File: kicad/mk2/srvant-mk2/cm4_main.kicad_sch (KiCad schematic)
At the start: 0 parts

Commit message: merge cm4 into one page, basic interconnection
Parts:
- added C19, C20: 10u 35v, Capacitor_SMD:C_0805_2012Metric, symbol Device:C
- added C21, C22, C24, C25, C26, C28, C58, C63, C64, C66, C68, C72, C73: 10u, Capacitor_SMD:C_0805_2012Metric, symbol Device:C
- added C23, C27, C29: 100n, Capacitor_SMD:C_0805_2012Metric, symbol Device:C
- added C35, C36, C37, C74, C75, C76 (x2), C77, C78, C79: 100n, Capacitor_SMD:C_0402_1005Metric, symbol Device:C
- added C62: 100u, Capacitor_Tantalum_SMD:CP_EIA-7343-31_Kemet-D, symbol Device:CP
- added C70, C71: 27p, Capacitor_SMD:C_0402_1005Metric, symbol Device:C
- added D2: LED Green, LED_SMD:LED_0603_1608Metric, symbol Device:LED
- added D3: LED Red, LED_SMD:LED_0603_1608Metric, symbol Device:LED
- added FB6: 220R, Resistor_SMD:R_0402_1005Metric, symbol Device:FerriteBead_Small
- added H1, H2, H3: MountingHole, MountingHole:MountingHole_2.5mm_Pad_TopOnly, symbol Mechanical:MountingHole
- added J2: Bus_M.2_Socket_M, footprints:1-2199230-5, symbol Connector:Bus_M.2_Socket_M
- added J3: HDMI connector, footprints:HDMI-10029449-001RLF, symbol CM4IO:HDMI_A_1.4
- added J3: Conn_02x05_Odd_Even, Connector_PinHeader_2.54mm:PinHeader_2x05_P2.54mm_Vertical, symbol Connector_Generic:Conn_02x05_Odd_Even
- added J4: ARJM11, Connector_RJ:RJ45_Wuerth_7499111446_Horizontal, symbol Connector:ARJM11
- added J4: 690-008-221-904, CM4:MOLEX_USB_67298-4090, symbol CM4IO:USB_67298-4090
- added L2: SRN6045TA-3R3Y, Inductor_SMD:L_Bourns_SRN6045TA, symbol pspice:INDUCTOR
- added Module1: ComputeModule4, CM4IO:Raspberry-Pi-4-Compute-Module, symbol CM4IO:ComputeModule4-CM4
- added R11, R12: 1K, Resistor_SMD:R_0402_1005Metric, symbol Device:R
- added R13, R14: 470R, Resistor_SMD:R_0402_1005Metric, symbol Device:R
- added R48: 15K/1%, Resistor_SMD:R_0402_1005Metric, symbol Device:R
- added R51, R52: 2.2K/1%, Resistor_SMD:R_0402_1005Metric, symbol Device:R
- added R53, R55, R56, R58: 36K/1%, Resistor_SMD:R_0402_1005Metric, symbol Device:R
- added R57: 12K/1%, Resistor_SMD:R_0402_1005Metric, symbol Device:R
- added R6: 100K 1%, Resistor_SMD:R_0402_1005Metric, symbol Device:R
- added R7: 22K 1%, Resistor_SMD:R_0402_1005Metric, symbol Device:R
- added TP4: TestPoint, TestPoint:TestPoint_Pad_1.5x1.5mm, symbol Connector:TestPoint
- added TP5, TP6, TP7, TP9: TestPoint, TestPoint:TestPoint_Pad_2.0x2.0mm, symbol Connector:TestPoint
- added U10: RT9742SNGV, Package_TO_SOT_SMD:SOT-23, symbol CM4IO:RT9742SNGV
- added U10: FSUSB42MUX, srvant:FSUSB42UMX, symbol CM4IO:FSUSB42MX
- added U11: USB2514B-I/M2, Package_DFN_QFN:QFN-36-1EP_6x6mm_P0.5mm_EP3.7x3.7mm, symbol Interface_USB:USB2514B_Bi
- added U3: TLV62585DRLR, TLV62585DRLR:DRL0006A, symbol TLV62585DRLR:TLV62585DRLR
- added U7: 74LVC1G07SE-7, Package_TO_SOT_SMD:SOT-353_SC-70-5, symbol CM4IO:74LVC1G07_copy
- added U8: AP22653W6, Package_TO_SOT_SMD:SOT-23-6, symbol CM4IO:AP2553W6
- added U8, U9: TPD4EUSB30, Package_SON:USON-10_2.5x1.0mm_P0.5mm, symbol CM4IO:TPD4EUSB30
- added Y2: 24MHz, srvant:LFXTAL-25MHz, symbol Device:Crystal_GND24
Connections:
- new net: R48.1, U8.5 (ILIM)
- new net: D3.1 (K), R12.1, TP9.1
- new net: J4.14 (LED1-), R14.1
- new net: J4.12 (LED2-), R13.1
- new net: C35.1, C76.1, J4.5 (CT), J4.6 (CT)
- new net: FB6.1, J4.SH
- new net: R55.1, U11.22 (SDA/SMBDATA/NON_REM1)
- new net: R51.2, R52.1, U10.2 (SEL)
- new net: L2.1, U3.2 (SW)
- new net: R12.2, U7.4
- new net: R57.2, U11.35 (RBIAS)
- new net: Module1.21 (PI_nLED_Activity), R11.2
- new net: D2.1 (K), R11.1
- new net: R56.1, U11.28 (SUSP_IND/LOCAL_PWR/NON_REM0)
- new net: R53.1, U11.24 (SCL/SMBCLK/CFG_SEL0)
- new net: R58.1, U11.25 (HS_IND/CFG_SEL1)
- new net +1.8v: Module1.88 (+1.8v_(Output)), Module1.90 (+1.8v_(Output))
- new net +3.3v: C72.1, C73.1, C74.1, C75.1, C76.1, C77.1, C78.1, C79.1, D2.2 (A), D3.2 (A), J4.11 (LED2+), J4.13 (LED1+), Module1.78 (GPIO_VREF(1.8v/3.3v_Input)), Module1.84 (+3.3v_(Output)), Module1.86 (+3.3v_(Output)), U10.1 (VCC), U11.10 (VDDA33), U11.15 (VDD33), U11.23 (VDD33), U11.27 (VBUS_DET), U11.29 (VDDA33), U11.36 (VDDA33), U11.5 (VDDA33), U7.5 (VCC)
- new net +3V3 PCIe: C21.1, C22.1, C23.1, C24.1, C25.1, C26.1, C27.1, C28.1, C29.1, J2.12 (3.3V), J2.14 (3.3V), J2.16 (3.3V), J2.18 (3.3V), J2.2 (3.3V), J2.4 (3.3V), J2.70 (3.3V), J2.72 (3.3V), J2.74 (3.3V), L2.2, R6.1, TP4.1
- new net +5v: C19.1, C20.1, C36.1, C58.1, Module1.77 (+5v_(Input)), Module1.79 (+5v_(Input)), Module1.81 (+5v_(Input)), Module1.83 (+5v_(Input)), Module1.85 (+5v_(Input)), Module1.87 (+5v_(Input)), U10.1 (IN), U3.3 (VIN), U3.4 (EN), U8.1 (IN)
- new net 3V3P_FB: R6.2, R7.1, TP5.1, U3.5 (FB)
- new net BT_nDis: Module1.91 (BT_nDisable)
- new net CAM0_C_N: Module1.140 (CAM0_C_N)
- new net CAM0_C_P: Module1.142 (CAM0_C_P)
- new net CAM0_D0_N: Module1.128 (CAM0_D0_N)
- new net CAM0_D0_P: Module1.130 (CAM0_D0_P)
- new net CAM0_D1_N: Module1.134 (CAM0_D1_N)
- new net CAM0_D1_P: Module1.136 (CAM0_D1_P)
- new net CAM1_C_N: Module1.127 (CAM1_C_N)
- new net CAM1_C_P: Module1.129 (CAM1_C_P)
- new net CAM1_D0_N: Module1.115 (CAM1_D0_N)
- new net CAM1_D0_P: Module1.117 (CAM1_D0_P)
- new net CAM1_D1_N: Module1.121 (CAM1_D1_N)
- new net CAM1_D1_P: Module1.123 (CAM1_D1_P)
- new net CAM1_D2_N: Module1.133 (CAM1_D2_N)
- new net CAM1_D2_P: Module1.135 (CAM1_D2_P)
- new net CAM1_D3_N: Module1.139 (CAM1_D3_N)
- new net CAM1_D3_P: Module1.141 (CAM1_D3_P)
- new net DSI0_C_N: Module1.169 (DSI0_C_N)
- new net DSI0_C_P: Module1.171 (DSI0_C_P)
- new net DSI0_D0_N: Module1.157 (DSI0_D0_N)
- new net DSI0_D0_P: Module1.159 (DSI0_D0_P)
- new net DSI0_D1_N: Module1.163 (DSI0_D1_N)
- new net DSI0_D1_P: Module1.165 (DSI0_D1_P)
- new net DSI1_C_N: Module1.187 (DSI1_C_N)
- new net DSI1_C_P: Module1.189 (DSI1_C_P)
- new net DSI1_D0_N: Module1.175 (DSI1_D0_N)
- new net DSI1_D0_P: Module1.177 (DSI1_D0_P)
- new net DSI1_D1_N: Module1.181 (DSI1_D1_N)
- new net DSI1_D1_P: Module1.183 (DSI1_D1_P)
- new net DSI1_D2_N: Module1.193 (DSI1_D2_N)
- new net DSI1_D2_P: Module1.195 (DSI1_D2_P)
- new net DSI1_D3_N: Module1.194 (DSI1_D3_N)
- new net DSI1_D3_P: Module1.196 (DSI1_D3_P)
- new net EEPROM_nWP: Module1.20 (EEPROM_nWP)
- new net ETH_LEDG: Module1.17 (Ethernet_nLED2(3.3v)), R13.2
- new net ETH_LEDY: Module1.15 (Ethernet_nLED3(3.3v)), R14.2
- new net GLOBAL_EN: Module1.99 (Global_EN)
- new net GND: C19.2, C20.2, C21.2, C22.2, C23.2, C24.2, C25.2, C26.2, C27.2, C28.2, C29.2, C35.2, C36.2, C37.2, C58.2, C62.2, C63.2, C64.2, C66.2, C68.2, C70.2, C71.2, C72.2, C73.2, C74.2, C75.2, C76.2, C76.2, C77.2, C78.2, C79.2, FB6.2, J2.1 (GND), J2.15 (GND), J2.21 (GND), J2.27 (GND), J2.3 (GND), J2.33 (GND), J2.39 (GND), J2.45 (GND), J2.51 (GND), J2.57 (GND), J2.71 (GND), J2.73 (GND), J2.75 (GND), J2.9 (GND), J3.11 (CKS), J3.17 (GND), J3.2 (D2S), J3.5 (D1S), J3.7 (Pin_7), J3.8 (D0S), J3.8 (Pin_8), J3.SH1 (SH), J3.SH2 (SH), J3.SH3 (SH), J3.SH4 (SH), J4.4 (GND`), J4.8 (GND), J4.MT1, J4.MT2, J4.MT3, J4.MT4, Module1.1 (GND), Module1.107 (GND), Module1.108 (GND), Module1.113 (GND), Module1.114 (GND), Module1.119 (GND), Module1.120 (GND), Module1.125 (GND), Module1.126 (GND), Module1.13 (GND), Module1.131 (GND), Module1.132 (GND), Module1.137 (GND), Module1.138 (GND), Module1.14 (GND), Module1.144 (GND), Module1.150 (GND), Module1.155 (GND), Module1.156 (GND), Module1.161 (GND), Module1.162 (GND), Module1.167 (GND), Module1.168 (GND), Module1.173 (GND), Module1.174 (GND), Module1.179 (GND), Module1.180 (GND), Module1.185 (GND), Module1.186 (GND), Module1.191 (GND), Module1.192 (GND), Module1.197 (GND), Module1.198 (GND), Module1.2 (GND), Module1.22 (GND), Module1.23 (GND), Module1.32 (GND), Module1.33 (GND), Module1.42 (GND), Module1.43 (GND), Module1.52 (GND), Module1.53 (GND), Module1.59 (GND), Module1.60 (GND), Module1.65 (GND), Module1.66 (GND), Module1.7 (GND), Module1.71 (GND), Module1.74 (GND), Module1.8 (GND), Module1.98 (GND), R48.2, R52.2, R53.2, R55.2, R56.2, R57.1, R58.2, R7.2, U10.10 (nOE), U10.3 (GND), U10.5 (GND), U11.37 (VSS), U3.1 (GND), U7.3 (GND), U8.2 (GND), U8.3 (GND), U8.8 (GND), U9.3 (GND), U9.8 (GND), Y2.2, Y2.4
- new net GPIO12: Module1.31 (GPIO12)
- new net GPIO13: Module1.28 (GPIO13)
- new net GPIO16: Module1.29 (GPIO16)
- new net GPIO17: Module1.50 (GPIO17)
- new net GPIO18: Module1.49 (GPIO18)
- new net GPIO19: Module1.26 (GPIO19)
- new net GPIO2: Module1.58 (GPIO2)
- new net GPIO20: Module1.27 (GPIO20)
- new net GPIO21: Module1.25 (GPIO21)
- new net GPIO22: Module1.46 (GPIO22)
- new net GPIO23: Module1.47 (GPIO23)
- new net GPIO24: Module1.45 (GPIO24)
- new net GPIO25: Module1.41 (GPIO25)
- new net GPIO26: Module1.24 (GPIO26)
- new net GPIO27: Module1.48 (GPIO27)
- new net GPIO3: Module1.56 (GPIO3)
- new net GPIO4: Module1.54 (GPIO4)
- new net GPIO5: Module1.34 (GPIO5)
- new net GPIO6: Module1.30 (GPIO6)
- new net GPIO7: Module1.37 (GPIO7)
- new net GPIO8: Module1.39 (GPIO8)
- new net GPIO9: Module1.40 (GPIO9)
- new net HD1_N: J4.2 (D-`), U11.1 (USBDM_DN1/PRT_DIS_M1)
- new net HD1_P: J4.3 (D+`), U11.2 (USBDP_DN1/PRT_DIS_P1)
- new net HD2_N: J4.6 (D-), U11.3 (USBDM_DN2/PRT_DIS_M2)
- new net HD2_P: J4.7 (D+), U11.4 (USBDP_DN2/PRT_DIS_P2)
- new net HD3_N: J3.3 (Pin_3), U11.6 (USBDM_DN3/PRT_DIS_M3)
- new net HD3_P: J3.5 (Pin_5), U11.7 (USBDP_DN3/PRT_DIS_P3)
- new net HD4_N: J3.4 (Pin_4), U11.8 (USBDM_DN4/PRT_DIS_M4)
- new net HD4_P: J3.6 (Pin_6), U11.9 (USBDP_DN4/PRT_DIS_P4)
- new net HDMI0_CEC: J3.13 (CEC), Module1.151 (HDMI0_CEC)
- new net HDMI0_CK_N: J3.12 (CK-), Module1.190 (HDMI0_CLK_N)
- new net HDMI0_CK_P: J3.10 (CK+), Module1.188 (HDMI0_CLK_P)
- new net HDMI0_D0_N: J3.9 (D0-), Module1.184 (HDMI0_TX0_N)
- new net HDMI0_D0_P: J3.7 (D0+), Module1.182 (HDMI0_TX0_P)
- new net HDMI0_D1_N: J3.6 (D1-), Module1.178 (HDMI0_TX1_N)
- new net HDMI0_D1_P: J3.4 (D1+), Module1.176 (HDMI0_TX1_P)
- new net HDMI0_D2_N: J3.3 (D2-), Module1.172 (HDMI0_TX2_N)
- new net HDMI0_D2_P: J3.1 (D2+), Module1.170 (HDMI0_TX2_P)
- new net HDMI0_HOTPLUG: J3.19 (HPD/HEAC-), Module1.153 (HDMI0_HOTPLUG)
- new net HDMI0_SCL: J3.15 (SCL), Module1.200 (HDMI0_SCL)
- new net HDMI0_SDA: J3.16 (SDA), Module1.199 (HDMI0_SDA)
- new net HDMI1_CEC: Module1.149 (HDMI1_CEC)
- new net HDMI1_CK_N: Module1.166 (HDMI1_CLK_N)
- new net HDMI1_CK_P: Module1.164 (HDMI1_CLK_P)
- new net HDMI1_D0_N: Module1.160 (HDMI1_TX0_N)
- new net HDMI1_D0_P: Module1.158 (HDMI1_TX0_P)
- new net HDMI1_D1_N: Module1.154 (HDMI1_TX1_N)
- new net HDMI1_D1_P: Module1.152 (HDMI1_TX1_P)
- new net HDMI1_D2_N: Module1.148 (HDMI1_TX2_N)
- new net HDMI1_D2_P: Module1.146 (HDMI1_TX2_P)
- new net HDMI1_HOTPLUG: Module1.143 (HDMI1_HOTPLUG)
- new net HDMI1_SCL: Module1.147 (HDMI1_SCL)
- new net HDMI1_SDA: Module1.145 (HDMI1_SDA)
- new net HDMI_5v: C37.1, J3.18 (+5V), U10.2 (OUT)
- new net HOST_RUN_PG: Module1.92 (RUN_PG)
- new net HOST_SCL_2: Module1.38 (GPIO11)
- new net HOST_SDA_2: Module1.44 (GPIO10)
- new net HOST_UART_RX: Module1.55 (GPIO14)
- new net HOST_UART_TX: Module1.51 (GPIO15)
- new net HOST_USB_N: U10.8 (HSD1_M)
- new net HOST_USB_P: U10.9 (HSD1_P)
- new net HOST_USB_SELECT: R51.1
- new net HOST_nRPIBOOT: Module1.93 (nRPIBOOT)
- new net ID_SC: Module1.35 (ID_SC)
- new net ID_SD: Module1.36 (ID_SD)
- new net PCIE_CLK_N: J2.53 (REFCLKn), Module1.112 (PCIe_CLK_N)
- new net PCIE_CLK_P: J2.55 (REFCLKp), Module1.110 (PCIe_CLK_P)
- new net PCIE_CLK_nREQ: J2.52 (~CLKREQ), Module1.102 (PCIe_CLK_nREQ)
- new net PCIE_RX_N: J2.41 (PERn0/SATA-B+), Module1.118 (PCIe_RX_N)
- new net PCIE_RX_P: J2.43 (PERp0/SATA-B-), Module1.116 (PCIe_RX_P)
- new net PCIE_TX_N: J2.47 (PETn0/SATA-A-), Module1.124 (PCIe_TX_N)
- new net PCIE_TX_P: J2.49 (PETp0/SATA-A+), Module1.122 (PCIe_TX_P)
- new net PCIE_nRST: J2.50 (~PERST), Module1.109 (PCIe_nRST)
- new net PCIe_nCLKREQ: TP6.1
- new net PCIe_nRST: TP7.1
- new net PWR1: U11.12 (PRTPWR1/BC_EN1), U8.3 (EN)
- new net SCL0: Module1.80 (SCL0)
- new net SDA0: Module1.82 (SDA0)
- new net SD_CLK: Module1.57 (SD_CLK)
- new net SD_DAT0: Module1.63 (SD_DAT0)
- new net SD_DAT1: Module1.67 (SD_DAT1)
- new net SD_DAT2: Module1.69 (SD_DAT2)
- new net SD_DAT3: Module1.61 (SD_DAT3)
- new net SD_PWR_ON: Module1.75 (SD_PWR_ON)
- new net SYNC_IN: Module1.16 (Ethernet_SYNC_IN(1.8v))
- new net SYNC_OUT: Module1.18 (Ethernet_SYNC_OUT(1.8v))
- new net TRD0_N: J4.2 (TD1-), Module1.10 (Ethernet_Pair0_N), U9.4 (D2+), U9.7
- new net TRD0_P: J4.1 (TD1+), Module1.12 (Ethernet_Pair0_P), U9.5 (D2-), U9.6
- new net TRD1_N: J4.4 (TD2-), Module1.6 (Ethernet_Pair1_N), U9.2 (D1-), U9.9
- new net TRD1_P: J4.3 (TD2+), Module1.4 (Ethernet_Pair1_P), U9.1 (D1+), U9.10
- new net TRD2_N: J4.8 (TD3-), Module1.9 (Ethernet_Pair2_N), U8.4 (D2+), U8.7
- new net TRD2_P: J4.7 (TD3+), Module1.11 (Ethernet_Pair2_P), U8.5 (D2-), U8.6
- new net TRD3_N: J4.10 (TD4-), Module1.5 (Ethernet_Pair3_N), U8.2 (D1-), U8.9
- new net TRD3_P: J4.9 (TD4+), Module1.3 (Ethernet_Pair3_P), U8.1 (D1+), U8.10
- new net TV_OUT: Module1.111 (VDAC_COMP)
- new net USB2_N: Module1.103 (USB2_N), U10.4 (D_N)
- new net USB2_P: Module1.105 (USB2_P), U10.3 (D_P)
- new net USBH_N: U10.6 (HSD0_M), U11.30 (USBDM_UP)
- new net USBH_P: U10.7 (HSD0_P), U11.31 (USBDP_UP)
- new net USBOTG_ID: Module1.101 (USB_OTG_ID)
- new net VBUS: C62.1, C63.1, C64.1, C66.1, C68.1, J3.1 (Pin_1), J3.2 (Pin_2), J4.1 (VBUS`), J4.5 (VBUS), U8.6 (OUT)
- new net WL_nDis: Module1.89 (WL_nDisable)
- new net XTALIN: C70.1, U11.33 (XTALIN/CLKIN), Y2.1
- new net XTALOUT: C71.1, U11.32 (XTALOUT), Y2.3
- new net nEXTRST: Module1.100 (nEXTRST), U11.26 (RESET_N)
- new net nOCS1: U11.13 (OCS_N1), U11.17 (OCS_N2), U11.19 (OCS_N3), U11.21 (OCS_N4), U8.4 (nFault)
- new net nPWR_LED: Module1.95 (nPI_LED_PWR), U7.2
- no-connect marks 0 -> 35
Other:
- removed sheet CM4_GPIO
- removed sheet cm4-high-speed
- note added: "3.3v @ 3A PSU For PCIE"
- note added: "Activity LED"
- note added: "Current Limit switch"
- note added: "Ethernet"
- note added: "Ethernet POE Protection"
- note added: "Expansion USB connector"
- note added: "HDMI power"
- note added: "M.2 Socket 3 (M-Key) PCIe x1"
- note added: "MOUNT HOLES"
- note added: "PCIe power"
- note added: "PWR LED"
- note added: "Stacked USB connectors"
- note added: "TESTPOINTS"
- note added: "TODO: EEPROM_nWP: use OR gate with the DIP switch and BMC pin BMC_HOST_USB_SELECT: use OR gate with the DIP switch and BMC pin"
- note added: "USB 2.0 Hub"
- note added: "USB power"

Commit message: more progress
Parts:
- removed R51: 2.2K/1%, Resistor_SMD:R_0402_1005Metric, symbol Device:R
- J7: renamed from J4; value 690-008-221-904 -> USB[690-008-221-904]; footprint CM4:MOLEX_USB_67298-4090 -> footprints:MOLEX_USB_67298-4090; Field4 Farnell -> (none); Field5 2751688 -> (none); Field6 690-008-221-904 -> (none); Field7 EDAC -> (none); Field8 UCON00727 -> (none); farnell# (none) -> 2751688
- U16: renamed from U10; footprint srvant:FSUSB42UMX -> footprints:FSUSB42UMX
- Y3: renamed from Y2; footprint srvant:LFXTAL-25MHz -> footprints:LFXTAL-25MHz
- renumbered C21 to C100, C27 to C101, C29 to C102, C23 to C103, C76 to C104, C35 to C105, C19 to C75, C58 to C76, C20 to C77, C36 to C78, C37 to C79, C62 to C80, C63 to C81, C64 to C82, C22 to C83, C66 to C84, C24 to C85, C68 to C86, C26 to C87, C70 to C88, C71 to C89, C72 to C90, C73 to C91, C74 to C92, C75 to C93, C76 to C94, C77 to C95, C78 to C96, C79 to C97, C25 to C98, C28 to C99, D2 to D7, D3 to D8, J3 to J10, J3 to J6, J2 to J8, J4 to J9, L2 to L3, R48 to R54, R6 to R55, R7 to R56, R52 to R58, R53 to R59, R11 to R60, R55 to R61, R56 to R62, R57 to R63, R58 to R64, R12 to R65, R13 to R66, R14 to R67, TP9 to TP11, TP4 to TP12, TP5 to TP13, TP6 to TP14, TP7 to TP15, U10 to U13, U8 to U14, U3 to U15, U11 to U17, U7 to U18, U8 to U19, U9 to U20
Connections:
- net USBOTG_ID is gone; now on net USB_DEMUX_SELECT: Module1.101 (USB_OTG_ID)
- net USB_DEMUX_SELECT: now reaches R58.1, U16.2 (SEL)
- net +3.3v renamed +3.3v_HOST
- net +5v renamed +5v_HOST
- net BT_nDis renamed HOST_BT_nDis
- net CAM0_C_N: no longer names the net of Module1.140 (CAM0_C_N)
- net CAM0_C_P: no longer names the net of Module1.142 (CAM0_C_P)
- net CAM0_D0_N: no longer names the net of Module1.128 (CAM0_D0_N)
- net CAM0_D0_P: no longer names the net of Module1.130 (CAM0_D0_P)
- net CAM0_D1_N: no longer names the net of Module1.134 (CAM0_D1_N)
- net CAM0_D1_P: no longer names the net of Module1.136 (CAM0_D1_P)
- net CAM1_C_N: no longer names the net of Module1.127 (CAM1_C_N)
- net CAM1_C_P: no longer names the net of Module1.129 (CAM1_C_P)
- net CAM1_D0_N: no longer names the net of Module1.115 (CAM1_D0_N)
- net CAM1_D0_P: no longer names the net of Module1.117 (CAM1_D0_P)
- net CAM1_D1_N: no longer names the net of Module1.121 (CAM1_D1_N)
- net CAM1_D1_P: no longer names the net of Module1.123 (CAM1_D1_P)
- net CAM1_D2_N: no longer names the net of Module1.133 (CAM1_D2_N)
- net CAM1_D2_P: no longer names the net of Module1.135 (CAM1_D2_P)
- net CAM1_D3_N: no longer names the net of Module1.139 (CAM1_D3_N)
- net CAM1_D3_P: no longer names the net of Module1.141 (CAM1_D3_P)
- net DSI0_C_N: no longer names the net of Module1.169 (DSI0_C_N)
- net DSI0_C_P: no longer names the net of Module1.171 (DSI0_C_P)
- net DSI0_D0_N: no longer names the net of Module1.157 (DSI0_D0_N)
- net DSI0_D0_P: no longer names the net of Module1.159 (DSI0_D0_P)
- net DSI0_D1_N: no longer names the net of Module1.163 (DSI0_D1_N)
- net DSI0_D1_P: no longer names the net of Module1.165 (DSI0_D1_P)
- net DSI1_C_N: no longer names the net of Module1.187 (DSI1_C_N)
- net DSI1_C_P: no longer names the net of Module1.189 (DSI1_C_P)
- net DSI1_D0_N: no longer names the net of Module1.175 (DSI1_D0_N)
- net DSI1_D0_P: no longer names the net of Module1.177 (DSI1_D0_P)
- net DSI1_D1_N: no longer names the net of Module1.181 (DSI1_D1_N)
- net DSI1_D1_P: no longer names the net of Module1.183 (DSI1_D1_P)
- net DSI1_D2_N: no longer names the net of Module1.193 (DSI1_D2_N)
- net DSI1_D2_P: no longer names the net of Module1.195 (DSI1_D2_P)
- net EEPROM_nWP renamed HOST_EEPROM_nWP
- net HDMI1_CEC: no longer names the net of Module1.149 (HDMI1_CEC)
- net HDMI1_CK_N: no longer names the net of Module1.166 (HDMI1_CLK_N)
- net HDMI1_CK_P: no longer names the net of Module1.164 (HDMI1_CLK_P)
- net HDMI1_D0_N: no longer names the net of Module1.160 (HDMI1_TX0_N)
- net HDMI1_D0_P: no longer names the net of Module1.158 (HDMI1_TX0_P)
- net HDMI1_D1_N: no longer names the net of Module1.154 (HDMI1_TX1_N)
- net HDMI1_D1_P: no longer names the net of Module1.152 (HDMI1_TX1_P)
- net HDMI1_D2_N: no longer names the net of Module1.148 (HDMI1_TX2_N)
- net HDMI1_D2_P: no longer names the net of Module1.146 (HDMI1_TX2_P)
- net HDMI1_HOTPLUG: no longer names the net of Module1.143 (HDMI1_HOTPLUG)
- net HDMI1_SCL: no longer names the net of Module1.147 (HDMI1_SCL)
- net HDMI1_SDA: no longer names the net of Module1.145 (HDMI1_SDA)
- net HOST_SCL_2 renamed HOST_I2C_SLAVE_SCL
- net HOST_SDA_2 renamed HOST_I2C_SLAVE_SDA
- net TV_OUT: no longer names the net of Module1.111 (VDAC_COMP)
- net WL_nDis renamed HOST_WL_nDis
- no-connect marks 35 -> 78
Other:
- note added: "Might remove the USB hub from the final version"
- note added: "Should FSUSB42MUX be powered by the "external" +3.3v provided by BMC (always ON) ?"
- moved on the sheet: R58, R66, R67

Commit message: save state
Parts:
- removed C76, C82, C83, C84, C85, C86, C87, C91: 10u, Capacitor_SMD:C_0805_2012Metric, symbol Device:C
- removed C78, C92, C93: 100n, Capacitor_SMD:C_0402_1005Metric, symbol Device:C
- removed C80: 100u, Capacitor_Tantalum_SMD:CP_EIA-7343-31_Kemet-D, symbol Device:CP
- removed J7: USB[690-008-221-904], footprints:MOLEX_USB_67298-4090, symbol CM4IO:USB_67298-4090
- removed L3: SRN6045TA-3R3Y, Inductor_SMD:L_Bourns_SRN6045TA, symbol pspice:INDUCTOR
- removed R54: 15K/1%, Resistor_SMD:R_0402_1005Metric, symbol Device:R
- removed R55: 100K 1%, Resistor_SMD:R_0402_1005Metric, symbol Device:R
- removed R56: 22K 1%, Resistor_SMD:R_0402_1005Metric, symbol Device:R
- removed R61, R62, R64: 36K/1%, Resistor_SMD:R_0402_1005Metric, symbol Device:R
- removed R63: 12K/1%, Resistor_SMD:R_0402_1005Metric, symbol Device:R
- removed TP13: TestPoint, TestPoint:TestPoint_Pad_2.0x2.0mm, symbol Connector:TestPoint
- removed U13: RT9742SNGV, Package_TO_SOT_SMD:SOT-23, symbol CM4IO:RT9742SNGV
- removed U15: TLV62585DRLR, TLV62585DRLR:DRL0006A, symbol TLV62585DRLR:TLV62585DRLR
- removed U17: USB2514B-I/M2, Package_DFN_QFN:QFN-36-1EP_6x6mm_P0.5mm_EP3.7x3.7mm, symbol Interface_USB:USB2514B_Bi
- removed Y3: 24MHz, footprints:LFXTAL-25MHz, symbol Device:Crystal_GND24
- added C70: 10u, Capacitor_SMD:C_0805_2012Metric, symbol Device:C
- added C74: 100u, Capacitor_Tantalum_SMD:CP_EIA-7343-31_Kemet-D, symbol Device:CP
- added FB6: 220R, Resistor_SMD:R_0402_1005Metric, symbol Device:FerriteBead_Small
- added J11: USB A, footprints:CONN_GSB19110KEU_AMP, symbol ARJM11:USB_A
- added R53: 15K/1%, Resistor_SMD:R_0402_1005Metric, symbol Device:R
- added R57: 510K 1%, Resistor_SMD:R_0402_1005Metric, symbol Device:R
- added TP18: ~, TestPoint:TestPoint_Pad_1.0x1.0mm, symbol Connector:TestPoint
- added U13: 74AHC1G04, Package_TO_SOT_SMD:SOT-23-5, symbol 74xGxx:74AHC1G04
- added U17: PCF85063AT/AAZ, Package_SO:SOIC-8_3.9x4.9mm_P1.27mm, symbol Timer_RTC:PCF8563T
- added U21: 74LVC1G07SE-7, Package_TO_SOT_SMD:SOT-353_SC-70-5, symbol CM4IO:74LVC1G07_copy
- added U23: SLB9670VQ20FW785XTMA1, QFN32_SLB9670VQ20FW785XTMA1_INF, symbol QFN32_SLB9670VQ20FW785XTMA1_INF:SLB9670VQ20FW785XTMA1
- added U25: 74AHC1G08, Package_TO_SOT_SMD:SOT-23-5_HandSoldering, symbol 74xGxx:74AHC1G08
- added Y3: X32K768S301, Crystal:Crystal_SMD_3215-2Pin_3.2x1.5mm, symbol Device:Crystal_Small
- C75, C77: value 10u 35v -> 10u; Field5 490-10505-1-ND -> 490-14381-1-ND; Field6 GRM21BC8YA106KE11L -> GRM21BR71A106KA73L; Field8 (none) -> 111893011; Part Description 10uF 10% or 20% 35V Ceramic Capacitor X6S 0805 (2012 Metric) -> 10uF 10% 10V Ceramic Capacitor X7R 0805 (2012 Metric)
- C79: value 100n -> 10u; footprint Capacitor_SMD:C_0402_1005Metric -> Capacitor_SMD:C_0805_2012Metric; Field4 Farnell -> Digikey; Field5 2611911 -> 490-14381-1-ND; Field6 RM EMK105 B7104KV-F -> GRM21BR71A106KA73L; Field7 TAIYO YUDEN EUROPE GMBH -> Murata; Field8 110091611 -> 111893011; Part Description 0.1uF 10% 16V Ceramic Capacitor X7R 0402 (1005 Metric) -> 10uF 10% 10V Ceramic Capacitor X7R 0805 (2012 Metric)
- C88, C89: value 27p -> 100n; Field4 Digikey -> Farnell; Field5 490-17672-1-ND -> 2611911; Field6 GJM1555C1H270JB01D -> RM EMK105 B7104KV-F; Field7 Murata -> TAIYO YUDEN EUROPE GMBH; Field8 UCAP00738 -> 110091611; Part Description 27pF 5% 50V Ceramic Capacitor C0G, NP0 0402 (1005 Metric) -> 0.1uF 10% 16V Ceramic Capacitor X7R 0402 (1005 Metric)
- C90: value 10u -> 100n; footprint Capacitor_SMD:C_0805_2012Metric -> Capacitor_SMD:C_0402_1005Metric; Field4 Digikey -> Farnell; Field5 490-14381-1-ND -> 2611911; Field6 GRM21BR71A106KA73L -> RM EMK105 B7104KV-F; Field7 Murata -> TAIYO YUDEN EUROPE GMBH; Field8 111893011 -> 110091611; Part Description 10uF 10% 10V Ceramic Capacitor X7R 0805 (2012 Metric) -> 0.1uF 10% 16V Ceramic Capacitor X7R 0402 (1005 Metric)
- C94: value 100n -> 1u; footprint Capacitor_SMD:C_0402_1005Metric -> Capacitor_SMD:C_0805_2012Metric; Field4 Farnell -> (none); Field5 2611911 -> (none); Field6 RM EMK105 B7104KV-F -> (none); Field7 TAIYO YUDEN EUROPE GMBH -> (none); Field8 110091611 -> (none); Part Description 0.1uF 10% 16V Ceramic Capacitor X7R 0402 (1005 Metric) -> (none)
- J6: now not fitted; now left out of the parts list
- R59: value 36K/1% -> 510K 1%; Field5 1458788 -> 1458807; Field6 MCR01MZPF3602 -> MCR01MZPF5103; Part Description Resistor 36K M1005 1% 63mW -> Resistor 510K M1005 1% 63mW
- TP11: footprint TestPoint:TestPoint_Pad_2.0x2.0mm -> TestPoint:TestPoint_Pad_D1.0mm
- TP12: value TestPoint -> 3v3_PCIe; footprint TestPoint:TestPoint_Pad_1.5x1.5mm -> TestPoint:TestPoint_Pad_D1.0mm
- TP14: value TestPoint -> PCIe_nCLKREQ; footprint TestPoint:TestPoint_Pad_2.0x2.0mm -> TestPoint:TestPoint_Pad_D1.0mm
- TP15: value TestPoint -> PCIe_nRST; footprint TestPoint:TestPoint_Pad_2.0x2.0mm -> TestPoint:TestPoint_Pad_D1.0mm
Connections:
- net HD3_N is gone; now on net +3.3v_HOST: J6.3 (Pin_3)
- net HD3_P is gone; now on net HOST_SCL5: J6.5 (Pin_5)
- net HD4_N is gone; now on net HOST_SPI4_SCLK: J6.4 (Pin_4)
- net HD4_P is gone; now on net HOST_SPI4_MOSI: J6.6 (Pin_6)
- net PCIe_nCLKREQ is gone; now on net PCIE_nRST: TP14.1
- net PCIe_nRST is gone; now on net PCIE_CLK_nREQ: TP15.1
- net XTALIN is gone; now on net +BATT: C88.1
- net XTALOUT is gone; now on net +5v_HOST: C89.1
- net +3.3v_HOST: now also C95.2, C96.2, C97.2, U23.1 (NCI/VDD), U23.14 (NCI/VDD), U23.22 (VDD), U23.8 (VDD); no longer C90.1, C95.1, C96.1, C97.1
- net +5v_HOST: now also J6.1 (Pin_1), R59.2, C70.1, R57.2, U13.5 (VCC), U21.5 (VCC), U25.5 (VCC); no longer C75.1, C77.1
- net +BATT: now also U17.8 (VDD)
- net GLOBAL_EN: now also U21.4
- net GND: now also C95.1, C96.1, C97.1, J6.10 (Pin_10), J6.9 (Pin_9), C70.2, C74.2, FB6.2, R53.2, U13.3 (GND), U17.4 (VSS), U21.3 (GND), U23.10 (NCI), U23.11 (NCI), U23.12 (NCI), U23.13 (NCI), U23.15 (NCI), U23.16 (NCI/GND), U23.2 (GND), U23.23 (GND), U23.25 (NCI), U23.26 (NCI), U23.27 (NCI), U23.28 (NCI), U23.29 (NCI), U23.3 (NCI), U23.32 (NCI), U23.33 (GND), U23.4 (NCI), U23.5 (NCI), U23.9 (GND), U25.3 (GND); no longer C90.2, C95.2, C96.2, C97.2, J6.7 (Pin_7), J6.8 (Pin_8), R59.2
- net GPIO25: now also U23.18 (PIRQ#)
- net USB_DEMUX_SELECT: now also U13.2
- net nEXTRST: now also U23.17 (RST#)
- net nOCS1: now also TP18.1
- net at U14.5 (ILIM): now also R53.1
- net at R59.1: now also C90.1, U21.2
- net +3V3 PCIe renamed +3.3v_HOST_PCIe
- net GPIO12 renamed HOST_SDA5
- net HOST_SDA5: now also J6.7 (Pin_7)
- net GPIO13 renamed HOST_SCL5
- net GPIO18 renamed HOST_SPI1_CE0_N
- net HOST_SPI1_CE0_N: now also U23.20 (CS#)
- net GPIO19 renamed HOST_SPI1_MISO
- net HOST_SPI1_MISO: now also U23.24 (MISO)
- net GPIO20 renamed HOST_SPI1_MOSI
- net HOST_SPI1_MOSI: now also U23.21 (MOSI)
- net GPIO21 renamed HOST_SPI1_SCLK
- net HOST_SPI1_SCLK: now also U23.19 (SCLK)
- net GPIO4 renamed HOST_SPI4_CE0
- net HOST_SPI4_CE0: now also J6.2 (Pin_2)
- net GPIO5 renamed HOST_SPI4_MISO
- net HOST_SPI4_MISO: now also J6.8 (Pin_8)
- net GPIO6 renamed HOST_SPI4_MOSI
- net GPIO7 renamed HOST_SPI4_SCLK
- net GPIO8 renamed HOST_UART4_TX
- net GPIO9 renamed HOST_UART4_RX
- net HDMI_5v renamed +5v_HOST_HDMI
- net +5v_HOST_HDMI: no longer C79.1
- net PWR1: no longer names the net of U14.3 (EN)
- net PWR1: now also U13.4
- net SCL0 renamed HOST_SCL0
- net HOST_SCL0: now also U17.6 (SCL)
- net SDA0 renamed HOST_SDA0
- net HOST_SDA0: now also U17.5 (SDA)
- net USBH_N renamed USB_OUT_N
- net USB_OUT_N: now also J11.2 (D-)
- net USBH_P renamed USB_OUT_P
- net USB_OUT_P: now also J11.3 (D+)
- net VBUS renamed +5v_HOST_VBUS
- net +5v_HOST_VBUS: now also C75.1, C77.1, C79.1, C74.1, J11.1 (VBUS); no longer J6.1 (Pin_1), J6.2 (Pin_2)
- new net: FB6.1, J11.4 (GND), J11.5 (Shield)
- new net: C90.2, R57.1, U25.4
- new net: U17.1 (OSCI), Y3.2
- new net: U17.2 (OSCO), Y3.1
- new net HOST_GLOBAL_EN: U25.2
- new net nRTC_INT: U17.3 (~{INT}), U25.1
- no-connect marks 78 -> 75
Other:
- note added: "DEV INTERFACE"
- note added: "EEPROM_nWP: pull this pin low to disable changing EEPROM BT_nDisable: When driven, or tied low, it prevents the Bluetooth module from powering u WL_nDisable: When driven or tied low it prevents the wireless network module from powering up."
- note added: "GLOBAL_EN needs to be pulse low for >1mS"
- note added: "HOST TPM 2.0 OPTIGA™ TPM SLB 9670 TPM2.0"
- note added: "HOST USB power"
- note added: "IIC address : 1010_001x"
- note added: "ROUTING: * HDMI signals should be routed as 100Ω differential pairs. Each signal within a pair should ideally be matched to better than 0.15mm. Pairs don't typically need any extra matching, as they only have to be matched to 25mm * USB: The differential pair should be routed as a 90Ω differential pair. The length of the P/N signals should ideally be matched to better than 0.15mm. * PCIE: The dif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"
- note added: "RTC alarms can be used to wake up the Compute module NB an Alarm triggering while already awake will cause a reset This can be used as a watchdog reset"
- note added: "RTC and RTC wakeup"
- note added: "TODO: nOCS1 WHERE? add TestPad to be able to solder wire"
- note added: "TPM signal PINs"
- note added: "The above circuit generates a pulse for GLOBAL_EN when nRTC_INT goes low"
- note added: "The differential Ethernet signals should be routed as 100Ω differential pairs, with suitable clearances. Length matching between pairs should be better than 50mm, so in the typical case no length matching is required. However the signals within a pair need to be length matched, ideally to better than 0.15mm."
- note added: "can I use another i2c on RPI? instead of 80/82 pins?"
- note added: "control USB host power by inverting DEMUX signal from BMC"
- note added: "place close to VDD/GND pins"
- note added: "some schematic/pinouts https://pinout.xyz/pinout/letstrust_tpm# https://www.letstrust.de/uploads/letstrust-v2.0.schematic.pdf"
- note removed: "3.3v @ 3A PSU For PCIE"
- note removed: "Expansion USB connector"
- note removed: "HDMI power"
- note removed: "Might remove the USB hub from the final version"
- note removed: "PCIe power"
- note removed: "Stacked USB connectors"
- note removed: "TODO: EEPROM_nWP: use OR gate with the DIP switch and BMC pin BMC_HOST_USB_SELECT: use OR gate with the DIP switch and BMC pin"
- note removed: "USB 2.0 Hub"
- note removed: "USB power"
- moved on the sheet: D7, Module1A, Module1B, R58, R60, TP15, U16

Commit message: mostly wired, impedance control, etc
Repositioned most of the components. Set impedance control based
on jlcpcb calculator.

Need to:
* reposition ethernet port to allow mounting hole.
* move power socket lower, reduce board size
* fix the rest of DRC errors.
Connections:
- net TRD1_N: now also J9.3 (TD2+); no longer J9.4 (TD2-)
- net TRD1_P: now also J9.4 (TD2-); no longer J9.3 (TD2+)
- net TRD3_N: now also J9.9 (TD4+); no longer J9.10 (TD4-)
- net TRD3_P: now also J9.10 (TD4-); no longer J9.9 (TD4+)
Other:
- note added: "swapped: 3/4 and 9/10"

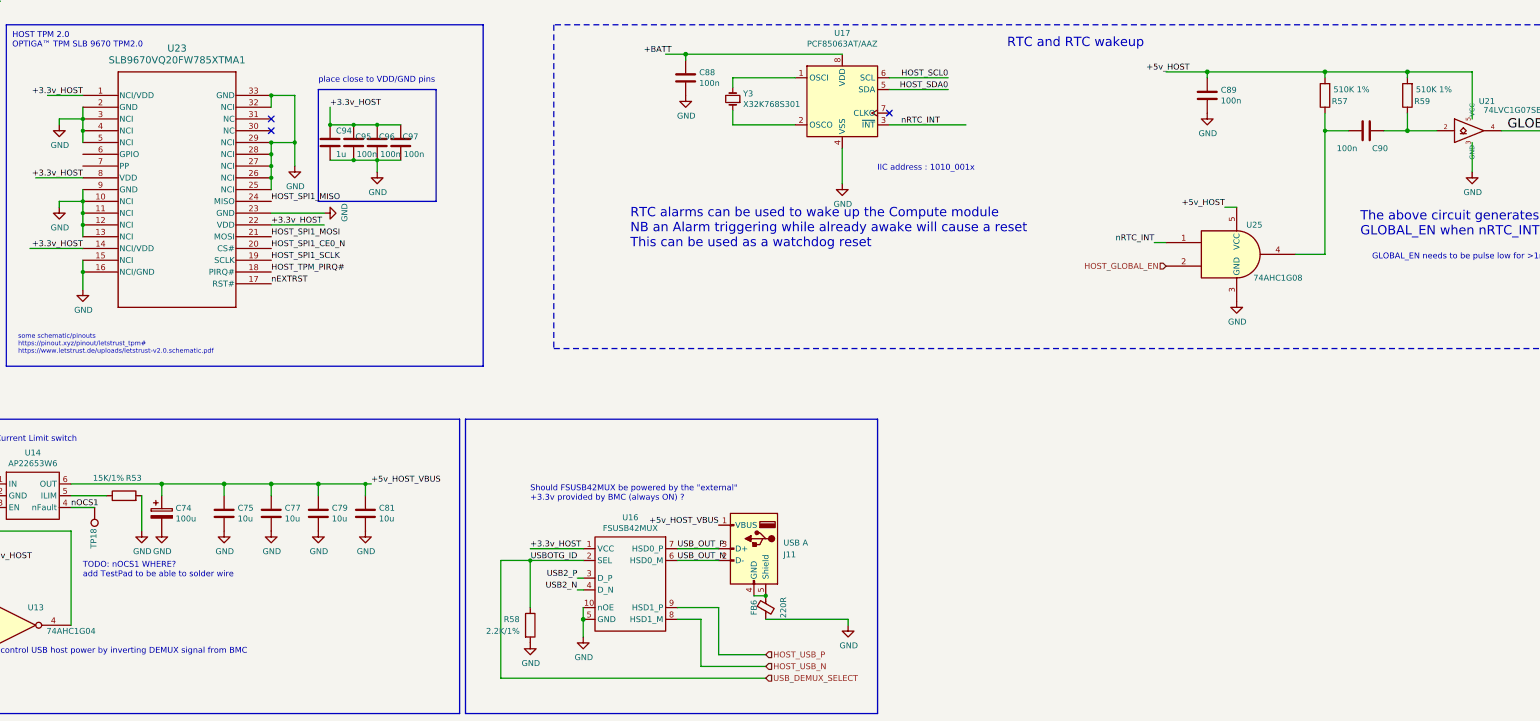
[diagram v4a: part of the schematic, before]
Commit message: fix descriptions, add 3dmodels.
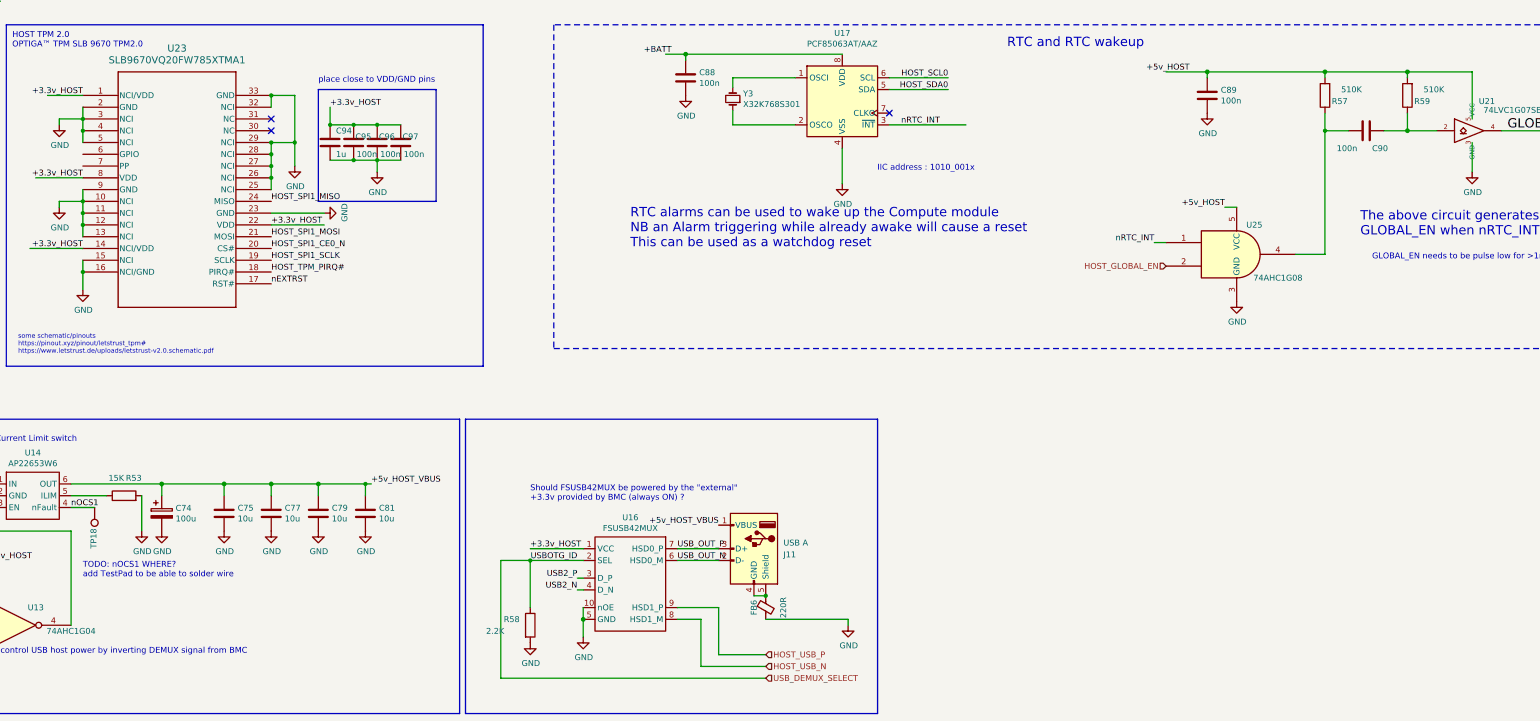
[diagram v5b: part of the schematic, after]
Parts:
- C100, C70, C75, C77, C79, C81, C98, C99: Part Description 10uF 10% 10V Ceramic Capacitor X7R 0805 (2012 Metric) -> 10uF 10% 10V Ceramic Capacitor X7R 0805 (2012 Metric)
- C101, C102, C103, C104, C105, C88, C89, C90, C95, C96, C97: Part Description 0.1uF 10% 16V Ceramic Capacitor X7R 0402 (1005 Metric) -> 0.1uF 10% 16V Ceramic Capacitor X7R 0402 (1005 Metric)
- D7: Part Description Green 572nm LED Indication - Discrete 2.2V 2-SMD, No Lead -> Green 572nm LED Indication - Discrete 2.2V 2-SMD, No Lead
- D8: Part Description Red 620nm LED Indication - Discrete 2.2V 2-SMD, No Lead -> Red 620nm LED Indication - Discrete 2.2V 2-SMD, No Lead
- Module1: Part Description 100 Position Connector Receptacle, Center Strip Contacts Surface Mount Gold -> 100 Position Connector Receptacle, Center Strip Contacts Surface Mount Gold
- R53: value 15K/1% -> 15K
- R57, R59: value 510K 1% -> 510K
- R58: value 2.2K/1% -> 2.2K
- U14: Part Description Power Switch/Driver 1:1 P-Channel 2.1A SOT-23-6 -> Power Switch/Driver 1:1 P-Channel 2.1A SOT-23-6
